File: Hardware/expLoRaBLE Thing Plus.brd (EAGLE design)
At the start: 22.9 x 58.4 mm, 138 parts, among them J2 CORTEX_DEBUG, J5 USB-C, J8 U.FL, U1 MCP73831, U2 3.3V, U3 NM180100, U4 CH340E_MSOP10, U6 DPX202700DT-4162A1, Y1 32.768kHz

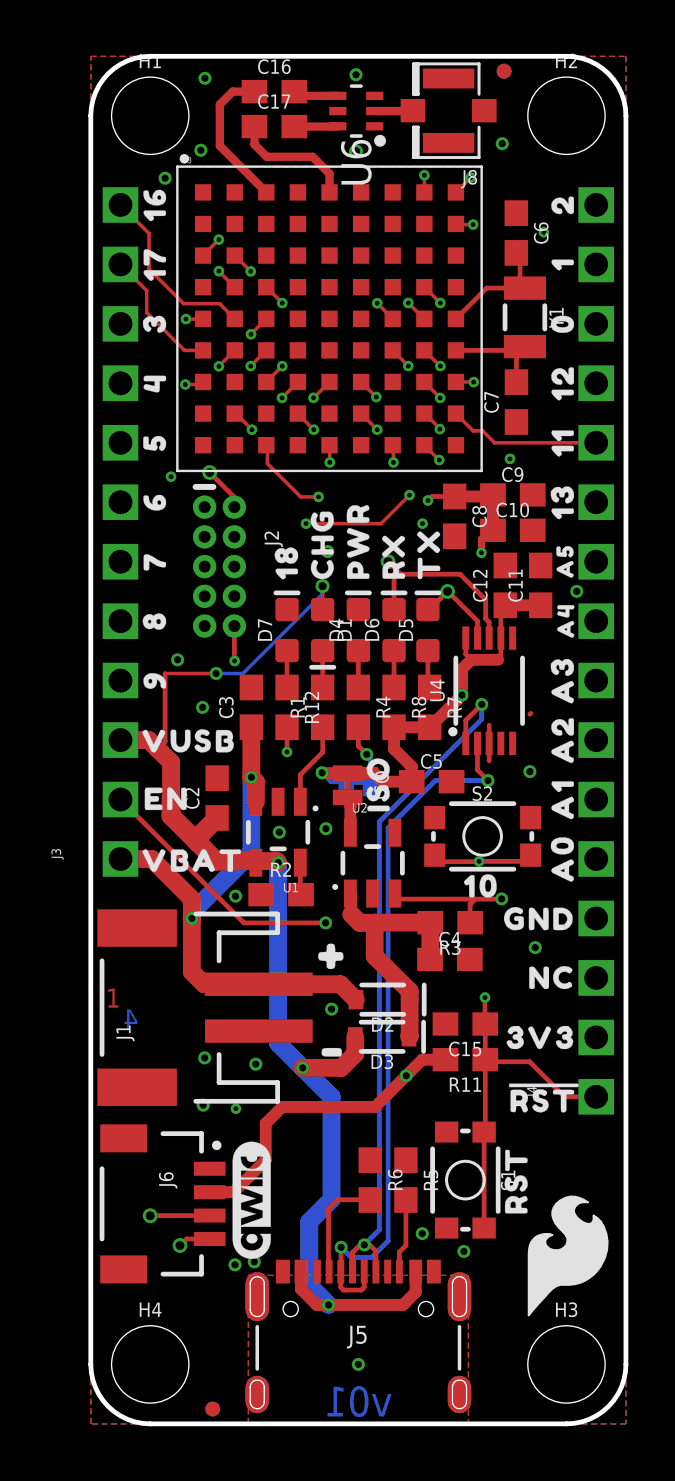
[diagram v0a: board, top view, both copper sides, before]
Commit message: Made changes per review meeting, added FCC ID
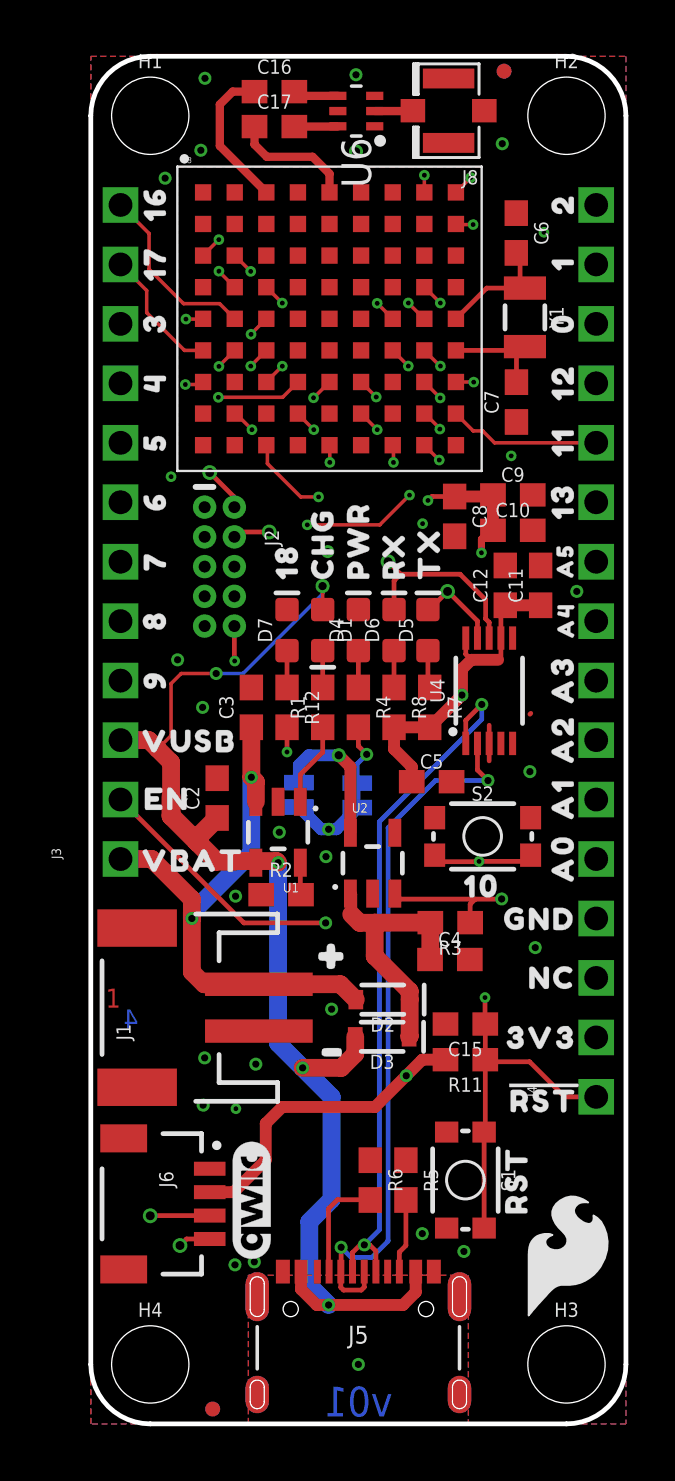
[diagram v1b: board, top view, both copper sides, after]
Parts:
- added TP6: TEST-POINTTP_15TH_THRU, SparkFun-Connectors:TP_15TH
- ISO: value JUMPER-SMT_2_NC_TRACE_NO-SILK -> JUMPER-SMT_2_NC_TRACE_SILK; device SparkFun-Jumpers:SMT-JUMPER_2_NC_TRACE_NO-SILK -> SparkFun-Jumpers:SMT-JUMPER_2_NC_TRACE_SILK
- moved U$33 3.75 mm to (8.89, 28.9), flipped to the bottom, turned to 0 degrees
- moved ISO 2.12 mm to (8.89, 26.9), flipped to the bottom, turned to 90 degrees
- moved LED 0.59 mm to (11.4, 26.8), turned to 270 degrees
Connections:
- net SWDCK: now also TP6.P$1
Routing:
- net N$14: track 1.56 -> 6.14 mm, vias 0 -> 1
- net 3.3V: track 44.6 -> 42.7 mm
- net ~D18/LED: track 25.8 -> 24.3 mm
- net ~D12/MISO: track 16.6 -> 15.8 mm
- net ~D9/A7: track 27.1 -> 26.3 mm
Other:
- board text added: "Contains FCC ID: 2AL5J-180100 Contains IC: 22729-180100"

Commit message: Design review changes
-Updated EN on bottom silk to be input <EN]
-Updated RESET on bottom silk to be input [!RESET!>
-Repositioned LED jumper buzzard label
-changed ISO jumper buzzard label to match inverted text style
-Updated RX and TX bottom labels to input/output flag type
-changed FCC info labels to buzzard
-updated A0-A5 bottom labels to include digital pin number as well.
-approved jumper drc errors
-nudged D18 trace on layer 15 to allow for ground pour to connect
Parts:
- removed U$24: (no value), output:#A3#0
- removed U$25: (no value), output:#A2#0
- removed U$26: (no value), output:#A1#0
- removed U$27: (no value), output:#A0#0
- added U$34: (no value), output:#ISO#0
- added U$35: (no value), output:#A1#20#0
- added U$36: (no value), output:#A2#21#0
- added U$37: (no value), output:#A3#22#0
- added U$38: (no value), output:#A4#23#0
- added U$39: (no value), output:#A5#24#0
- U$22: device output:#A5#0 -> output:CONTAINS_FCC_ID#_2AL5J#1801000
- U$23: device output:#A4#0 -> output:CONTAINS_IC#_22729#1801000
- U$33: device output:ISO0 -> output:#A0#19#0
- moved U$33 13.1 mm to (21.1, 24.1)
- moved U$23 11.8 mm to (10.5, 39.6), turned to 90 degrees
- moved U$22 9.82 mm to (11.7, 39.5), turned to 90 degrees
- moved U$32 1.65 mm to (11.4, 26.0), turned to 90 degrees
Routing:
- net ~D18/LED: track 24.3 -> 24.9 mm
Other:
- board text removed: "Contains FCC ID: 2AL5J-180100 Contains IC: 22729-180100"
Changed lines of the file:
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@@
 <drawing>
 <settings>
-<setting alwaysvectorfont="no"/>
+<setting alwaysvectorfont="yes"/>
 <setting verticaltext="up"/>
 </settings>
 <grid distance="0.05" unitdist="inch" unit="inch" style="lines" multiple="1" display="yes" altdistance="0.001" altunitdist="inch" altunit="inch"/>
 <layers>
-<layer number="1" name="Top" color="4" fill="1" visible="no" active="yes"/>
+<layer number="1" name="Top" color="4" fill="1" visible="yes" active="yes"/>
 <layer number="2" name="Route2" color="11" fill="3" visible="no" active="yes"/>
 <layer number="3" name="Route3" color="17" fill="1" visible="no" active="no"/>
@@
 <layer number="47" name="Measures" color="7" fill="1" visible="no" active="yes"/>
 <layer number="48" name="Document" color="7" fill="1" visible="no" active="yes"/>
-<layer number="49" name="Reference" color="7" fill="1" visible="no" active="yes"/>
+<layer number="49" name="Reference" color="7" fill="1" visible="yes" active="yes"/>
 <layer number="50" name="dxf" color="7" fill="1" visible="no" active="no"/>
 <layer number="51" name="tDocu" color="6" fill="1" visible="yes" active="yes"/>
@@
 </layers>
 <board>
-<fusionsync huburn="a.YnVzaW5lc3M6Z21haWwxMTI2MzE1" projecturn="a.YnVzaW5lc3M6Z21haWwxMTI2MzE1I0QyMDIwMDgzMTMyODE1ODgwNg" f3durn="urn:adsk.wipprod:dm.lineage:mHH6g35GTyuWC89OADwm_A" pcbguid="" lastpulledtime="" lastsyncedchangeguid="" latestrevisionid="c9279973-d255-4697-9a7c-0f6c20acbc86" lastsyncedrevisionid="c9279973-d255-4697-9a7c-0f6c20acbc86" lastboardhashguid="e8377822-6ace-51a9-b550-49c57cccff0e" lastpushedtime="2020-10-21T19:52:57Z" linktopcb3d="true"/>
+<fusionsync huburn="a.YnVzaW5lc3M6Z21haWwxMTI2MzE1" projecturn="a.YnVzaW5lc3M6Z21haWwxMTI2MzE1I0QyMDIwMDgzMTMyODE1ODgwNg" f3durn="urn:adsk.wipprod:dm.lineage:mHH6g35GTyuWC89OADwm_A" pcbguid="" lastpulledtime="" lastsyncedchangeguid="" latestrevisionid="c9279973-d255-4697-9a7c-0f6c20acbc86" lastsyncedrevisionid="c9279973-d255-4697-9a7c-0f6c20acbc86" lastboardhashguid="e8377822-6ace-51a9-b550-49c57cccff0e" lastpushedtime="2020-10-21T19:52:57Z" linktopcb3d="false"/>
 <plain>
 <wire x1="0" y1="55.88" x2="0" y2="2.54" width="0.2032" layer="20"/>
@@
 <text x="0.635" y="16.891" size="0.8128" layer="15" font="vector" ratio="25">3</text>
 <text x="2.032" y="16.891" size="0.8128" layer="16" font="vector" ratio="25" rot="MR0">4</text>
-<text x="8.89" y="39.37" size="0.6096" layer="22" font="vector" rot="MR270" align="center">Contains FCC ID: 2AL5J-180100
-Contains IC: 22729-180100</text>
 </plain>
 <attributes>
@@
 <element name="U$20" library="output" package="#11#COPI#0" value="" x="21.1074" y="41.91" smashed="yes" rot="MR0"/>
 <element name="U$21" library="output" package="#13#SCK#0" value="" x="21.1074" y="39.37" smashed="yes" rot="MR0"/>
-<element name="U$22" library="output" package="#A5#0" value="" x="21.1074" y="36.83" smashed="yes" rot="MR0"/>
-<element name="U$23" library="output" package="#A4#0" value="" x="21.1074" y="34.29" smashed="yes" rot="MR0"/>
-<element name="U$24" library="output" package="#A3#0" value="" x="21.1074" y="31.75" smashed="yes" rot="MR0"/>
-<element name="U$25" library="output" package="#A2#0" value="" x="21.1074" y="29.21" smashed="yes" rot="MR0"/>
-<element name="U$26" library="output" package="#A1#0" value="" x="21.1074" y="26.67" smashed="yes" rot="MR0"/>
-<element name="U$27" library="output" package="#A0#0" value="" x="21.1074" y="24.13" smashed="yes" rot="MR0"/>
 <element name="U$28" library="output" package="#GND#0" value="" x="21.1074" y="21.59" smashed="yes" rot="MR0"/>
 <element name="U$29" library="output" package="#NC#0" value="" x="21.1074" y="19.05" smashed="yes" rot="MR0"/>
 <element name="U$30" library="output" package="#3V3#0" value="" x="21.1074" y="16.51" smashed="yes" rot="MR0"/>
 <element name="U$31" library="output" package="##RESET##0" value="" x="21.1074" y="13.97" smashed="yes" rot="MR0"/>
-<element name="U$32" library="output" package="#LED#0" value="" x="12.2174" y="27.432" smashed="yes" rot="MR0"/>
+<element name="U$32" library="output" package="#LED#0" value="" x="11.3792" y="26.0096" smashed="yes" rot="MR90"/>
 <element name="ISO" library="SparkFun-Jumpers" package="SMT-JUMPER_2_NC_TRACE_SILK" package3d_urn="urn:adsk.eagle:package:39281/1" value="JUMPER-SMT_2_NC_TRACE_SILK" x="8.89" y="26.8732" smashed="yes" rot="MR90">
 <attribute name="NAME" x="10.033" y="26.8732" size="0.6096" layer="26" font="vector" ratio="20" rot="MR90" align="bottom-center"/>
 <attribute name="VALUE" x="7.747" y="26.8732" size="0.6096" layer="28" font="vector" ratio="20" rot="MR90" align="top-center"/>
 </element>
-<element name="U$33" library="output" package="ISO0" value="" x="8.89" y="28.9306" smashed="yes" rot="MR0"/>
 <element name="LOGO4" library="SparkFun-Aesthetics" package="ORDERING_INSTRUCTIONS" value="SPECIAL_INSTRUCTIONS-ORDERING" x="-33.02" y="-21.59" smashed="yes"/>
 <element name="TP6" library="SparkFun-Connectors" library_urn="urn:adsk.eagle:library:513" package="TP_15TH" package3d_urn="urn:adsk.eagle:package:38288/1" value="TEST-POINTTP_15TH_THRU" x="7.62" y="38.1" smashed="yes"/>
+<element name="U$34" library="output" package="#ISO#0" value="" x="8.8392" y="26.035" smashed="yes" rot="MR90"/>
+<element name="U$33" library="output" package="#A0#19#0" value="" x="21.1074" y="24.13" smashed="yes" rot="MR0"/>
+<element name="U$35" library="output" package="#A1#20#0" value="" x="21.1074" y="26.67" smashed="yes" rot="MR0"/>
+<element name="U$36" library="output" package="#A2#21#0" value="" x="21.1074" y="29.21" smashed="yes" rot="MR0"/>
+<element name="U$37" library="output" package="#A3#22#0" value="" x="21.1074" y="31.75" smashed="yes" rot="MR0"/>
+<element name="U$38" library="output" package="#A4#23#0" value="" x="21.1074" y="34.29" smashed="yes" rot="MR0"/>
+<element name="U$39" library="output" package="#A5#24#0" value="" x="21.1074" y="36.83" smashed="yes" rot="MR0"/>
+<element name="U$22" library="output" package="CONTAINS_FCC_ID#_2AL5J#1801000" value="" x="11.6586" y="39.5224" smashed="yes" rot="MR90"/>
+<element name="U$23" library="output" package="CONTAINS_IC#_22729#1801000" value="" x="10.541" y="39.5732" smashed="yes" rot="MR90"/>
 </elements>
 <signals>
@@
 <wire x1="6.8326" y1="45.1866" x2="6.834175" y2="45.185025" width="0.1524" layer="1"/>
 <via x="6.834175" y="45.185025" extent="1-16" drill="0.2032"/>
-<wire x1="6.834175" y1="45.185025" x2="6.834175" y2="44.753225" width="0.1524" layer="15"/>
-<wire x1="6.834175" y1="44.753225" x2="7.0612" y2="44.5262" width="0.1524" layer="15"/>
 <wire x1="11.0236" y1="44.24786875" x2="11.0236" y2="29.9212" width="0.1524" layer="15"/>
 <wire x1="9.8044" y1="28.702" x2="11.0236" y2="29.9212" width="0.1524" layer="15"/>
 <wire x1="9.8044" y1="28.702" x2="8.382" y2="28.702" width="0.1524" layer="15"/>
-<wire x1="7.0612" y1="44.5262" x2="10.74526875" y2="44.5262" width="0.1524" layer="15"/>
+<wire x1="8.7376" y1="43.8912" x2="7.5946" y2="43.8912" width="0.1524" layer="15"/>
+<wire x1="8.7376" y1="43.8912" x2="9.3726" y2="44.5262" width="0.1524" layer="15"/>
+<wire x1="9.3726" y1="44.5262" x2="10.74526875" y2="44.5262" width="0.1524" layer="15"/>
 <wire x1="10.74526875" y1="44.5262" x2="11.0236" y2="44.24786875" width="0.1524" layer="15"/>
+<wire x1="7.5946" y1="43.8912" x2="6.834175" y2="44.651625" width="0.1524" layer="15"/>
+<wire x1="6.834175" y1="44.651625" x2="6.834175" y2="45.185025" width="0.1524" layer="15"/>
 </signal>
 <signal name="~D20/A1">
@@
 </drawing>
 <compatibility>
-<note version="6.3" minversion="6.2.2" severity="warning">
-Since Version 6.2.2 text objects can contain more than one line,
-which will not be processed correctly with this version.
-</note>
 <note version="8.2" severity="warning">
 Since Version 8.2, EAGLE supports online libraries. The ids

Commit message: RX/TX labels back to rounded, some minor tweaks to layer 15 for better gnd flow
-fixed one right angle on layer 15, net D9/A7
-nudged some traces and vias to allow for better ground flow on all pours
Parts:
- moved C2 0.63 mm to (4.97, 26.3)
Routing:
- net ~D18/LED: track 24.9 -> 22.1 mm, vias 2 -> 3
- net !RESET: track 60.1 -> 62.2 mm, vias 3 -> 4
- net ~D23/A4: track 21.5 -> 20.1 mm
- net D10/SWCH: track 27.6 -> 26.3 mm
- net ~D5: track 11.3 -> 10.0 mm
- net D-1: track 30.5 -> 29.3 mm
- net RXI-0: track 25.0 -> 23.9 mm
- net ~D4: track 5.58 -> 4.67 mm
- net V_USB: track 55.0 -> 55.8 mm
- net V_BATT: track 24.7 -> 25.4 mm
- net ~D19/A0: track 26.1 -> 25.5 mm
- net 3.3V: track 42.7 -> 43.3 mm
- net ~D9/A7: track 26.3 -> 25.7 mm
- net ~D20/A1: track 22.6 -> 22.0 mm
- net ~D6: track 10.2 -> 9.61 mm
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
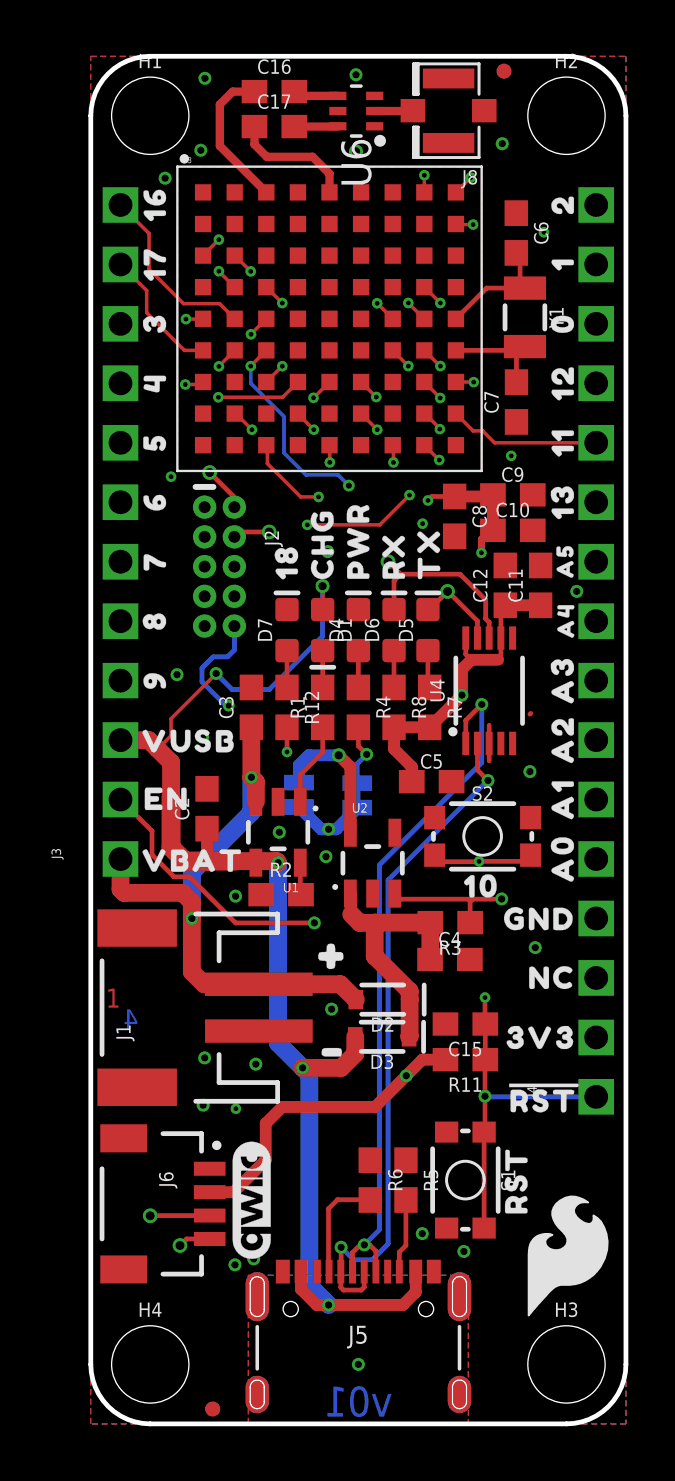
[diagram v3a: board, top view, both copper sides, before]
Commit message: Added NO jumper for RTS - RESET
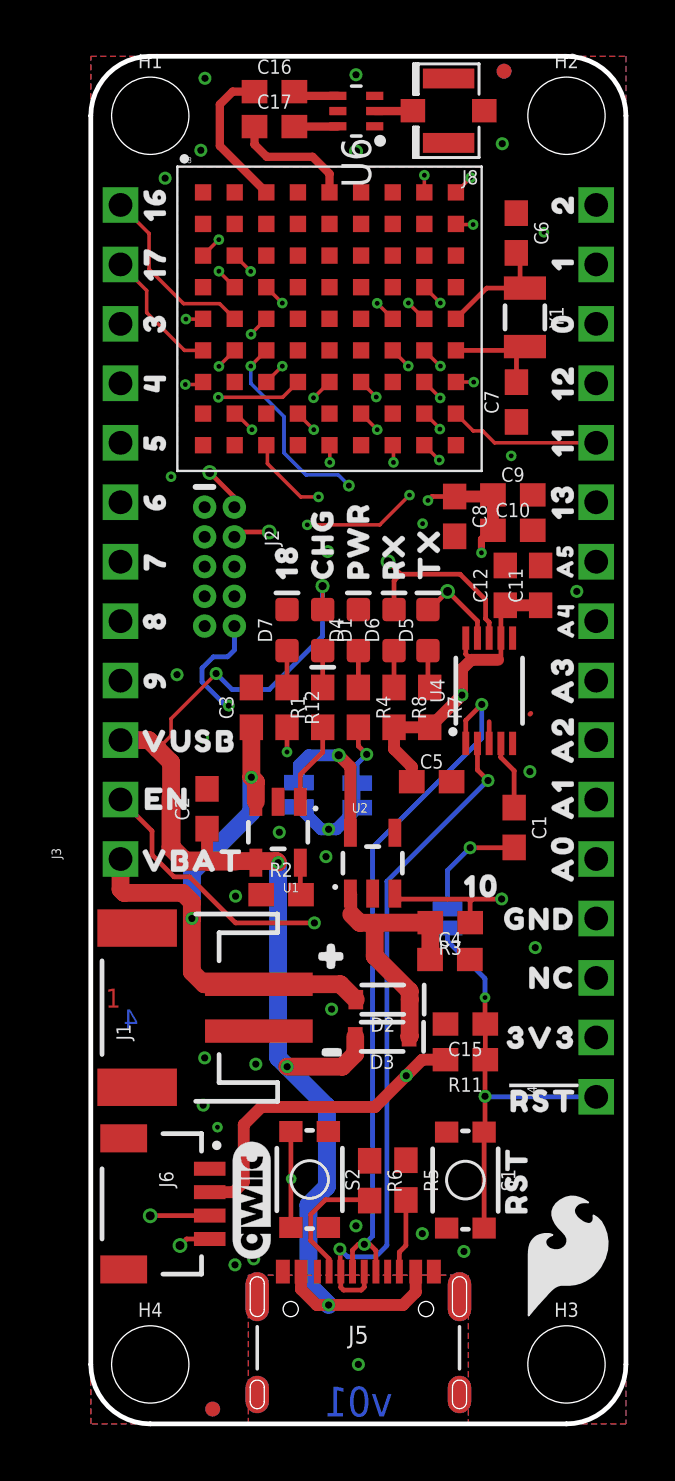
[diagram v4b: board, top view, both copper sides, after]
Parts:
- added C1: 0.1uF, SparkFun-Capacitors:0603
- added JP1: JUMPER-SMT_2_NO_SILK, SparkFun-Jumpers:SMT-JUMPER_2_NO_SILK
- moved S2 16.4 mm to (9.35, 10.4), turned to 270 degrees
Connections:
- new net !RTS: C1.1, U4.4
- new net N$15: C1.2, JP1.1
- net !RESET: now also JP1.2
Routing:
- net D10/SWCH: track 26.3 -> 40.2 mm
- net N$15: track 0.00 -> 4.90 mm, vias 0 -> 1
- net !RESET: track 62.2 -> 65.6 mm
- net !RTS: track 0.00 -> 2.98 mm
- net V_USB: track 55.8 -> 57.0 mm
- net CC1: track 4.64 -> 5.56 mm
- net GND: track 1.58 -> 0.98 mm, vias 26 -> 27
- net 3.3V: track 43.3 -> 43.8 mm
